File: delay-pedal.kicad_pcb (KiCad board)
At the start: 2 copper layers, 50.8 x 88.9 mm, 61 parts, among them J1 9V IN: 1=+ 2=GND, J2 INPUT: 1=TIP 2=SLEEVE, J3 OUTPUT: 1=TIP 2=SLEEVE, J4 TIME B10k, J5 FEEDBACK B10k, J6 MIX B10k, J7 MOMENTARY NO, J8 LED: 1=A 2=K, K1 G5V-2-H1 DC5, Q1 2N3904, U1 LM7805_TO220, U3 MCP6002-I/P, U4 23LC1024-I/P

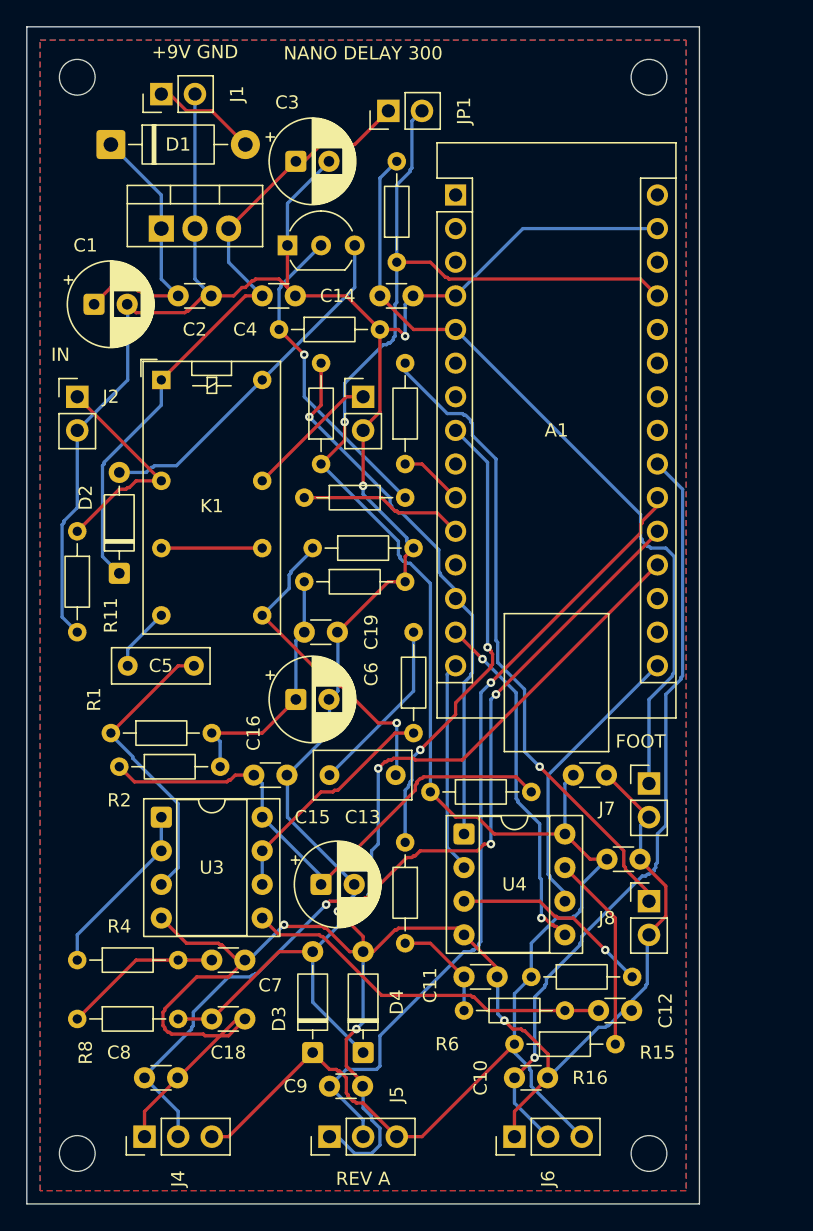
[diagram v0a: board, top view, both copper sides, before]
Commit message: Improve revision C PCB layout, labels and manufacturing documentation
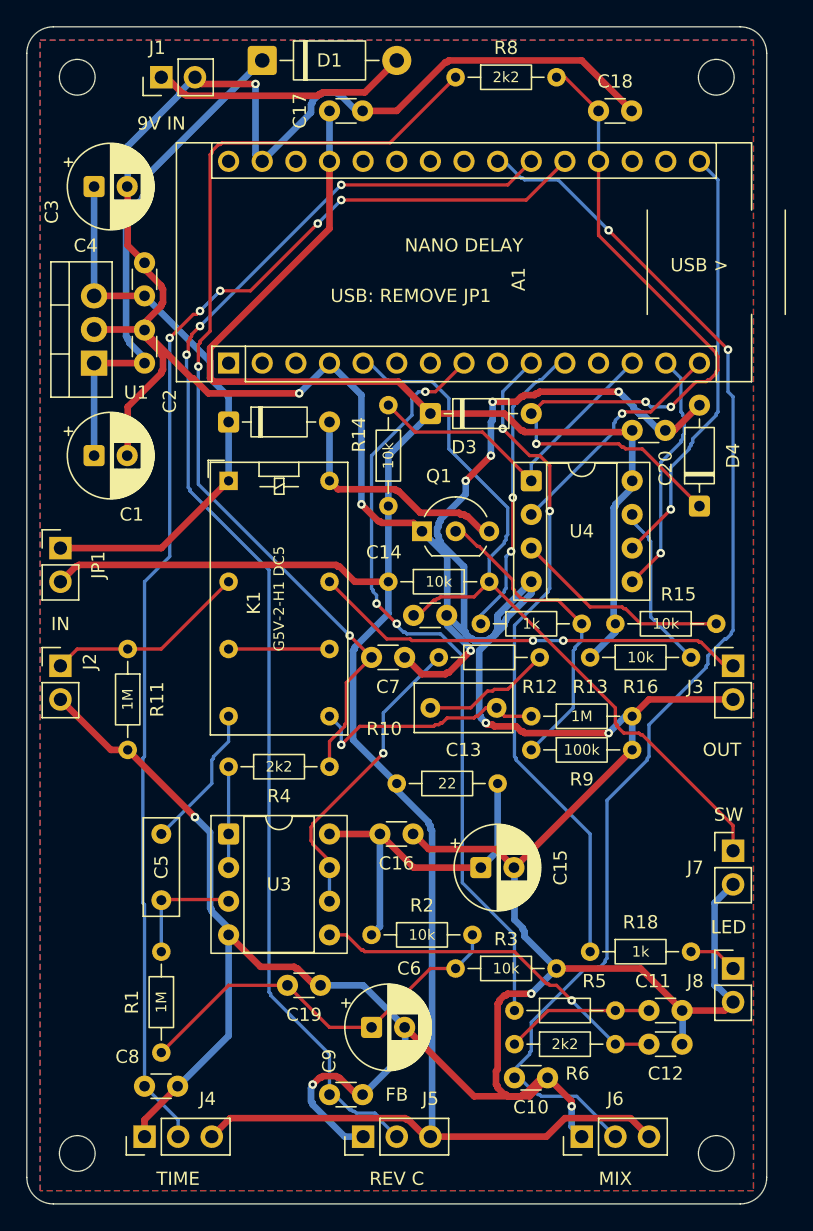
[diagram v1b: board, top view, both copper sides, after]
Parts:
- A1: footprint Module:Arduino_Nano -> Delay:Arduino_Nano_EdgeUSB
- H1, H2, H3, H4: footprint MountingHole_2.7mm_M2.5 -> MountingHole:MountingHole_2.7mm_M2.5
- moved R8 76.6 mm to (32.4, 3.81)
- moved C18 74.5 mm to (43.2, 6.35)
- moved C17 53.4 mm to (22.9, 6.35)
- moved D3 49.1 mm to (30.5, 29.2), turned to 0 degrees
- moved D4 48.5 mm to (50.8, 36.2)
- moved JP1 41.3 mm to (2.54, 39.4), turned to 0 degrees
- moved R18 39.4 mm to (42.5, 69.8), turned to 0 degrees
- moved R9 37.0 mm to (38.1, 54.6)
- moved J3 34.5 mm to (53.3, 48.3)
- moved C20 32.4 mm to (45.7, 30.5)
- moved R3 31.4 mm to (32.4, 71.1)
- moved R16 29.8 mm to (42.5, 47.6)
- moved R15 27.4 mm to (44.5, 45.1)
- moved U4 27.1 mm to (38.1, 34.3)
- moved C19 26.7 mm to (19.7, 72.4)
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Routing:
- net /GND: track 286.8 -> 395.0 mm, vias 6 -> 14
- net /ADC_F1: track 12.0 -> 74.4 mm, vias 0 -> 2
- net /LED_CTRL: track 4.86 -> 50.7 mm, vias 0 -> 2
- net /LED_ANODE: track 49.0 -> 3.70 mm, vias 1 -> 0
- net /5V_LOGIC: track 157.8 -> 196.8 mm, vias 1 -> 0
- net /FEEDBACK: track 61.3 -> 99.6 mm, vias 1 -> 3
- net /MIX: track 58.2 -> 95.5 mm, vias 1 -> 2
- net /TIME: track 68.5 -> 97.6 mm, vias 3 -> 5
- net /PWM_OUT: track 35.0 -> 58.6 mm, vias 2 -> 3
- net /OUTPUT: track 10.3 -> 33.1 mm, vias 0 -> 2
- net /9V_PROT: track 20.7 -> 38.5 mm
- net /SRAM_CS: track 41.5 -> 25.2 mm, vias 1 -> 0
- net /5V_ANALOG: track 41.2 -> 27.2 mm
- net /BUF_IN: track 22.4 -> 9.16 mm
- net /9V_IN: track 7.93 -> 19.5 mm
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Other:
- board size 50.8 x 88.9 mm -> 55.9 x 88.9 mm
- board text added: "9V IN"
- board text added: "A1 NANO v3"
- board text added: "C1 47u 25V"
- board text added: "C10 100n"
- board text added: "C11 10n"
- board text added: "C12 10n"
- board text added: "C13 1u"
- board text added: "C14 100n"
- board text added: "C15 100u 16V"
- board text added: "C16 100n"
- board text added: "C17 100n"
- board text added: "C18 10n"
- board text added: "C19 100n"
- board text added: "C2 330n"
- board text added: "C20 100n"
- board text added: "C3 47u 16V"
- board text added: "C4 100n"
- board text added: "C5 100n"
- board text added: "C6 47u 16V"
- board text added: "C7 10n"
- board text added: "C8 100n"
- board text added: "C9 100n"
- board text added: "D1 1N4007"
- board text added: "D2 1N4148"
- board text added: "D3 BAT85"
- board text added: "D4 BAT85"
- board text added: "J1 9V IN 1 +9V 2 GND"
- board text added: "J2 IN 1T 2G"
- board text added: "J3 OUTPUT 1 TIP 2 GND"
- board text added: "J4 TIME B10k 1G 2W 3+5"
- board text added: "J5 FB B10k 1G 2W 3+5"
- board text added: "J6 MIX B10k 1G 2W 3+5"
- board text added: "J7 SWITCH 1 SW 2 GND"
- board text added: "J8 LED 1+ 2-"
- board text added: "JP1 PWR LINK REMOVE FOR USB"
- board text added: "K1 G5V-2-H1 5V COIL"
- board text added: "NANO DELAY"
- board text added: "Q1 2N3904"
- board text added: "R1 1M"
- board text added: "R10 22"
- board text added: "R11 1M"
- board text added: "R12 100"
- board text added: "R13 1M"
- board text added: "R14 10k"
- board text added: "R15 10k"
- board text added: "R16 10k"
- board text added: "R17 10k"
- board text added: "R18 1k"
- board text added: "R2 10k"
- board text added: "R3 10k"
- board text added: "R4 2k2"
- board text added: "R5 2k2"
- board text added: "R6 2k2"
- board text added: "R7 1k"
- board text added: "R8 2k2"
- board text added: "R9 100k"
- board text added: "REV C"
- board text added: "REV C | 55.88 x 88.90 mm | R2 corners | 4 x 2.70 mm NPTH 2 layers / 1.6 mm FR4 | Signal 0.25 mm / Power 0.50 mm / Clearance 0.20 mm"
- board text added: "SW"
- board text added: "U1 7805"
- board text added: "U3 MCP6002"
- board text added: "U4 23LC1024"
- board text added: "USB >"
- board text removed: "+9V GND"
- board text removed: "9V + -"
- board text removed: "9V regulated / center-negative jack wired off board"
- board text removed: "All pots: 1=GND 2=W 3=+5V"
- board text removed: "FOOT"
- board text removed: "NANO DELAY 300"
- board text removed: "REV A"
- board text removed: "REV A / PROTOTYPE"

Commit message: rev c renewed
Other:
- board text added: "NANO DELAY barlasardic"
- board text added: "barlasardic"
- board text removed: "NANO DELAY"
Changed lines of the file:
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@@
 		)
 	)
-	(gr_text "NANO DELAY"
-		(at 33.02 16.51 0)
+	(gr_text "NANO DELAY\nbarlasardic"
+		(at 33 15 0)
 		(layer "F.SilkS")
 		(effects
@@
 		)
 	)
+	(gr_text "barlasardic"
+		(at 31.5 7.5 0)
+		(layer "F.SilkS")
+		(effects
+			(font
+				(size 1 1)
+				(thickness 0.15)
+			)
+			(justify left bottom)
+		)
+	)
